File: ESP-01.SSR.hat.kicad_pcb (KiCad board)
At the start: 2 copper layers, 45.7 x 50.8 mm, 11 parts, among them J1 Screw_Terminal_01x06, J4 Screw_Terminal_01x04, K1 G3MB-202P, K2 G3MB-202P, Q1 BC547, Q2 BC547, U1 ESP-01v090, U2 AMS1117-3.3

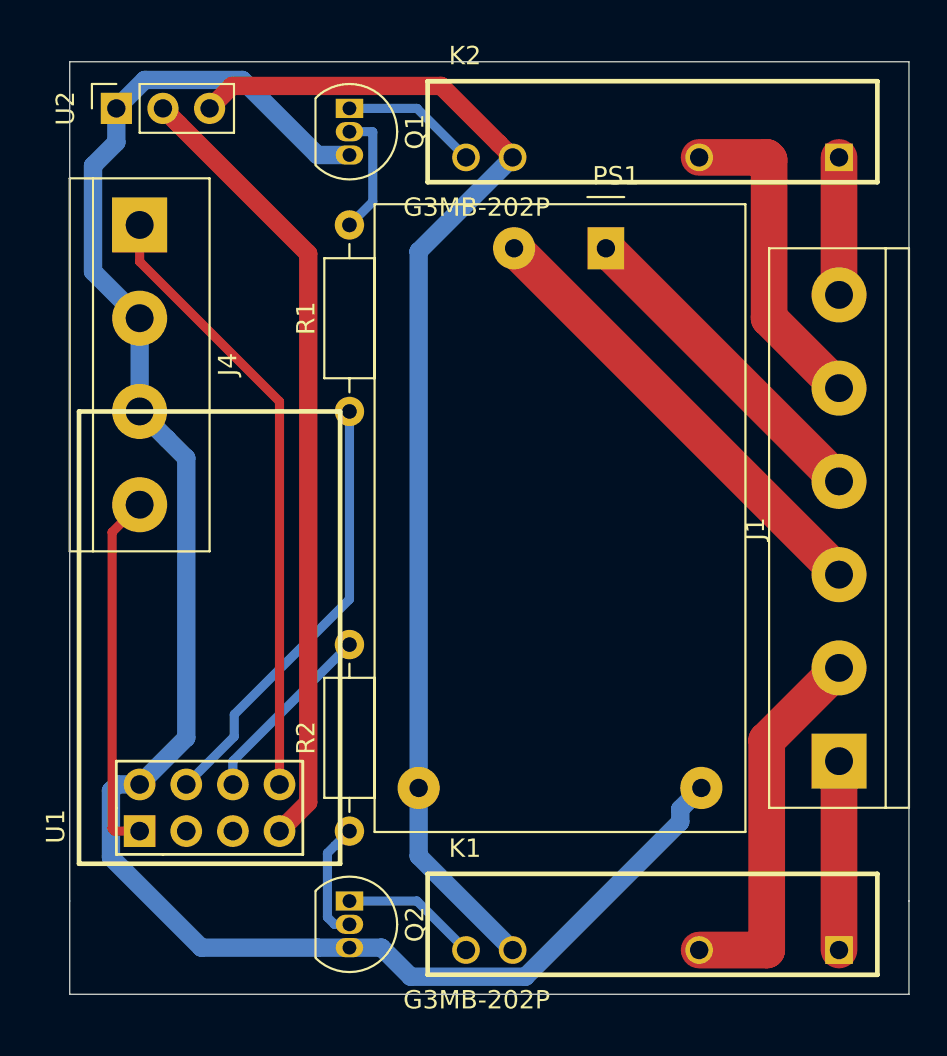
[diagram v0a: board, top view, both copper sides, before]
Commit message: shifted and moved elements
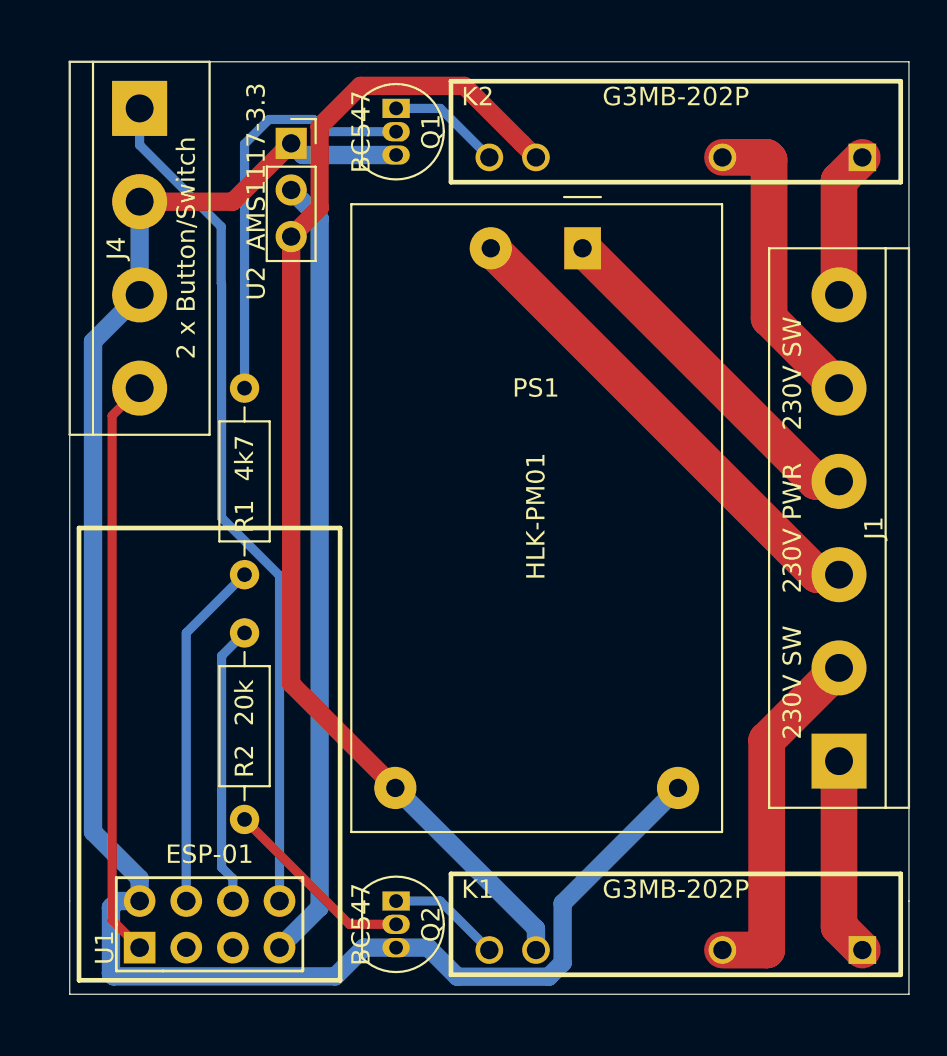
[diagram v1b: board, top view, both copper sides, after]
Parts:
- J1: value Screw_Terminal_01x06 -> 230V SW 230V PWR 230V SW
- J4: value Screw_Terminal_01x04 -> 2 x Button/Switch
- U1: value ESP-01v090 -> ESP-01
- moved R1 10.6 mm to (177.2, 52.1)
- moved U2 9.71 mm to (179.7, 28.6), turned to 0 degrees
- moved J4 6.35 mm to (171.4, 26.7)
- moved U1 6.35 mm to (171.4, 72.4)
- moved R2 5.75 mm to (177.2, 65.4)
- moved Q1 2.54 mm to (185.4, 26.7)
- moved Q2 2.54 mm to (185.4, 69.8)
- moved K1 1.27 mm to (200.7, 71.1)
- moved K2 1.27 mm to (200.7, 27.9)
- moved PS1 1.27 mm to (195.6, 34.3)
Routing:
- net Net-(Q1-Pad2): track 6.86 -> 23.1 mm
- net Net-(J4-Pad1): track 33.6 -> 46.3 mm
- net Net-(J4-Pad4): track 19.8 -> 31.7 mm
- net Net-(R2-Pad2): track 10.3 -> 15.4 mm
- net Net-(R1-Pad1): track 24.0 -> 19.1 mm
- net Net-(Q2-Pad2): track 6.55 -> 10.6 mm
- net Net-(J1-Pad3): track 25.1 -> 26.4 mm
- net Net-(J1-Pad4): track 18.0 -> 19.2 mm
- net Net-(K2-Pad4): track 7.46 -> 6.19 mm
- net Net-(K1-Pad4): track 7.46 -> 6.19 mm
- net Net-(J1-Pad5): track 17.9 -> 16.6 mm
- net Net-(J1-Pad2): track 20.7 -> 19.4 mm
- net GND: track 100.4 -> 99.5 mm
- net +5V: track 66.1 -> 65.3 mm
- net Net-(J1-Pad1): track 10.3 -> 10.8 mm
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
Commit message: final
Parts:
- J1: value 230V SW 230V PWR 230V SW -> Screw_Terminal_01x06
- J4: value 2 x Button/Switch -> Screw_Terminal_01x04
- U1: value ESP-01 -> ESP-01v090
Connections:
- J1 pad 2: Net-(J1-Pad2) -> AC
- J1 pad 3: Net-(J1-Pad3) -> Earth
- J1 pad 4: Net-(J1-Pad4) -> AC
- J1 pad 6: Net-(J1-Pad6) -> AC
- K1 pad 2: Net-(J1-Pad2) -> Earth
- K2 pad 1: Net-(J1-Pad6) -> Net-(J1-Pad5)
- K2 pad 2: Net-(J1-Pad5) -> Earth
- PS1 pad 1: Net-(J1-Pad4) -> AC
- PS1 pad 2: Net-(J1-Pad3) -> Earth
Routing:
- net Earth: track 0.00 -> 63.3 mm
- net AC: track 0.00 -> 39.8 mm
- net Net-(J1-Pad3): track 26.4 -> 0.00 mm
- net Net-(J1-Pad2): track 19.4 -> 0.00 mm
- net Net-(J1-Pad4): track 19.2 -> 0.00 mm
- net Net-(J1-Pad6): track 8.02 -> 0.00 mm
- net Net-(J1-Pad5): track 16.6 -> 15.3 mm
